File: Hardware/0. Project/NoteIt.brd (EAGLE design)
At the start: 50 x 50 mm, 61 parts, among them CN1 USB 3.2 Gen 2 Type C Receptac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, CN3 Micro-SD Card, CN4 FTSH-105-01-L-DV-K-TR, CN6 Lithium Ion Polymer, IC5 S-8261ACMMD-G4MT2U, Q1 SI2374DS, Q2 SI2374DS, SW1 KY-040, U1 SN74AHC1G125DBV, U2 GL823K, U3 TLV75530PDBVR, U4 TS3A27518EPWR, U8 DS3231/SO

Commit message: board design wip
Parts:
- moved Q1 33.6 mm to (29.0, 25.2), flipped to the bottom
- moved Q2 26.5 mm to (28.7, 29.4), flipped to the bottom
- moved Q4 26.0 mm to (23.4, 22.5), flipped to the bottom
- moved X2 22.4 mm to (28.8, 19.6), turned to 270 degrees
- moved IC2 21.2 mm to (23.9, 25.7), flipped to the bottom, turned to 90 degrees
- moved IC5 20.6 mm to (19.0, 28.9), flipped to the bottom
- moved U1 20.3 mm to (18.8, 23.6), flipped to the bottom
- moved U3 15.2 mm to (23.7, 29.4), flipped to the bottom

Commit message: board design wip
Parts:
- removed CN2: (no value), con-ptr500:AK500/2-H
- added P1: OSTTE020104, Terminal Block 2P 3.5pitch:OST_OSTTE020104
- moved CN4 20.7 mm to (40.5, 17.3)
- moved CN6 16.1 mm to (42.3, 29.6), turned to 270 degrees
- moved U2 15.7 mm to (30.3, 12.0)
- moved U4 13.1 mm to (23.2, 8.77), turned to 180 degrees
- moved SW1 6.78 mm to (40.9, 17.7), turned to 180 degrees
- moved BAT1 6.22 mm to (17.7, 9.16)
- moved CN3 6.22 mm to (8.66, 17.0)
- moved IC2 6.22 mm to (24.1, 19.5)
- moved IC5 6.22 mm to (19.3, 22.7)
- moved Q1 6.22 mm to (29.2, 19.0)
- moved Q4 6.22 mm to (23.7, 16.3)
- moved U1 6.22 mm to (19.1, 17.4)
- moved U10 6.22 mm to (24.9, 21.7)
- moved U3 6.22 mm to (24.0, 23.2)
- moved U8 6.22 mm to (12.6, 21.7)
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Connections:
- net 0V: now also P1.2; no longer CN2.2
- net N$4: now also P1.1; no longer CN2.1
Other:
- board size 50 x 50 mm -> 50 x 35 mm

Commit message: Board design WIP
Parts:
- removed BAT1: CR1220, SamacSys_Parts:1072
- removed P1: OSTTE020104, Terminal Block 2P 3.5pitch:OST_OSTTE020104
- added C12: (no value), My-RLC:C0603
- added CN11: CR1220, SamacSys_Parts:1072
- added CN14: OSTTE020104, Terminal Block 2P 3.5pitch:OST_OSTTE020104
- added R16, R19, R20: (no value), My-RLC:R0603
- moved R6 103.7 mm to (8.26, 1.56), flipped to the bottom
- moved C13 98.4 mm to (8.26, 3.15), flipped to the bottom, turned to 180 degrees
- moved R8 89.9 mm to (18.3, 24.1)
- moved C25 87.4 mm to (11.7, 26.4), flipped to the bottom, turned to 270 degrees
- moved R7 85.9 mm to (18.3, 25.7)
- moved C14 84.8 mm to (12.5, 14.6), turned to 180 degrees
- moved C21 79.3 mm to (18.3, 22.6), turned to 180 degrees
- moved C5 77.8 mm to (18.3, 21.0), turned to 180 degrees
- moved C16 76.6 mm to (35.2, 2.54), flipped to the bottom, turned to 90 degrees
- moved C2 73.2 mm to (26.6, 24.9)
- moved R22 72.4 mm to (15.0, 26.4), flipped to the bottom, turned to 270 degrees
- moved C6 70.5 mm to (26.6, 27.4)
- moved C7 68.7 mm to (33.6, 2.54), flipped to the bottom, turned to 90 degrees
- moved C3 66.6 mm to (16.8, 15.0), flipped to the bottom, turned to 90 degrees
- moved LED2 64.7 mm to (47.6, 7.59), flipped to the bottom, turned to 270 degrees
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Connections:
- net 0V: now also C12.2, CN11.-, CN14.2; no longer BAT1.-, P1.2
- net 3.3V: now also C12.1, R16.1, R19.1, R20.1
- net GPIO_ROTARY_ENCODER_BUTTON: now also R16.2
- net GPIO_ROTARY_ENCODER_SIGNAL_A: now also R19.2
- net GPIO_ROTARY_ENCODER_SIGNAL_B: now also R20.2
- net N$22: now also CN11.+; no longer BAT1.+
- net N$4: now also CN14.1; no longer P1.1
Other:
- board text added: "+"
- board text added: "-"

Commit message: NoteIt v1.0 release
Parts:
- removed C25, C39: (no value), My-RLC:C0603
- removed CN14: OSTTE020104, Terminal Block 2P 3.5pitch:OST_OSTTE020104
- removed IC2: (no value), adafruit:SOT23-5L
- removed IC5: S-8261ACMMD-G4MT2U, SamacSys_Parts:SOT95P275X135-6N
- removed Q4: (no value), transistor-npn:SOT23-BEC
- removed R41, R42: (no value), My-RLC:R0603
- removed U10: (no value), MSP430FR2476TPTR:QFP50P900X900X160-48N
- added C17, C20: 100nF, My-RLC:C0603
- added CN2: Lithium Ion Polymer, Battery:JST-PH-2-SMT-RA
- added Q3: SI2374DS, SI2374DS:SOT-23(TO-236)
- added R21, R23: 10k (5%), My-RLC:R0603
- added U5: SN74AHC1G125DBV, SN74AHC1G125DRLR:SOT23-5
- added U6: TS3A27518EPWR, TS3A27518EPWR:SOP65P640X120-24N
- added U7: TLV75530PDBVR, TLV75530PDBVR:SOT23-5L
- C1: value (none) -> 10uF x 10V
- C10, C5: value (none) -> 10uF
- C11, C12, C15, C16, C19, C2, C21, C4, C6, C7: value (none) -> 100nF
- C13: value (none) -> 1nF x 50V
- C14, C18: value (none) -> 1uF
- C3: value (none) -> 4.7nF
- C8, C9: value (none) -> 22pF x 100V
- CN3: value Micro-SD Card -> (none); device Micro SD:MICROSD-PUSH-OUT -> Terminal Block 2P 3.5pitch:OST_OSTTE020104
- CN6: value Lithium Ion Polymer -> Micro-SD Card; device Battery:JST-PH-2-SMT-RA -> Micro SD:MICROSD-PUSH-OUT
- Q1: value SI2374DS -> BC817; device SI2374DS:SOT-23(TO-236) -> transistor-npn:SOT23-BEC
- R1, R15, R16, R2, R4: value (none) -> 1M
- R10, R19, R20: value (none) -> 4K7 (5%)
- R11: value (none) -> 4k7
- R12: value (none) -> 10k
- R13, R18, R22, R8: value (none) -> 10k (5%)
- R14: value (none) -> 1k (5%)
- R17: value (none) -> 47k (5%)
- R3, R6: value (none) -> 5k1 (5%)
- R5: value (none) -> 4K7
- R7: value (none) -> 2k
- R9: value (none) -> 470R
- U1: value SN74AHC1G125DBV -> MCP73831/2; device SN74AHC1G125DRLR:SOT23-5 -> adafruit:SOT23-5L
- U2: value GL823K -> MSP430FR2476TPTR; device SamacSys_Parts:SOP64P600X175-16N -> MSP430FR2476TPTR:QFP50P900X900X160-48N
- U3: value TLV75530PDBVR -> S-8261ACMMD-G4MT2U; device TLV75530PDBVR:SOT23-5L -> SamacSys_Parts:SOT95P275X135-6N
- U4: value TS3A27518EPWR -> GL823K; device TS3A27518EPWR:SOP65P640X120-24N -> SamacSys_Parts:SOP64P600X175-16N
- Y1: value (none) -> 32.768 kHz
- moved R17 40.1 mm to (8.26, 1.56)
- moved R9 39.8 mm to (15.0, 26.4), turned to 270 degrees
- moved CN3 35.5 mm to (41.0, 30.5), flipped to the top, turned to 180 degrees
- moved C1 32.6 mm to (17.9, 22.6), flipped to the top, turned to 180 degrees
- moved R12 32.1 mm to (47.6, 10.7), turned to 0 degrees
- moved C7 31.3 mm to (13.3, 26.4)
- moved R18 30.9 mm to (16.7, 9.50), turned to 270 degrees
- moved C15 30.8 mm to (18.8, 9.50), turned to 90 degrees
- moved R6 30.5 mm to (38.7, 2.54), turned to 270 degrees
- moved U1 30.2 mm to (17.9, 19.8), turned to 0 degrees
- moved C3 29.6 mm to (43.7, 2.54)
- moved R20 27.1 mm to (17.9, 24.2), flipped to the top, turned to 0 degrees
- moved R22 26.4 mm to (37.1, 11.9)
- moved R19 24.7 mm to (17.9, 25.8), flipped to the top, turned to 0 degrees
- moved C5 23.9 mm to (33.6, 2.54), flipped to the bottom, turned to 90 degrees
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- renumbered C24 to C18, CN11 to CN5, LED2 to LED1, X2 to Y1
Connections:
- net !CONNECT_SDCARD_TO_USB: now also Q1.C, R13.1, U6.14, U6.24; no longer Q4.C, R11.1, U4.14, U4.24
- net !GPIO_DISPLAY_RESET: now also U2.41; no longer U10.41
- net !SDCARD_CARD_DETECT!: now also CN6.9, R18.2, U2.18; no longer CN3.9, R5.2, U10.18
- net !SPI_DISPLAY_CS: now also U2.11; no longer U10.11
- net 0V: now also C1.2, C14.2, C16.2, C17.1, C20.1, C5.1, C6.1, C8.2, CN3.2, CN6.6, CN6.G1, CN6.G2, CN6.G3, CN6.G4, Q1.E, Q3.2, R16.1, R2.1, R4.2, R5.1, R6.2, R7.1, R8.2, U1.2, U2.48, U4.1, U4.14, U5.1, U5.3, U6.20, U6.5, U7.2; no longer C1.1, C14.1, C16.1, C25.2, C39.2, C5.2, C6.2, C7.1, CN14.2, CN3.6, CN3.G1, CN3.G2, CN3.G3, CN3.G4, IC2.2, Q2.2, Q4.E, R1.2, R13.1, R15.2, R18.1, R2.2, R42.1, R9.1, U1.1, U1.3, U10.48, U2.1, U2.14, U3.2, U4.20, U4.5
- net 3.3V: now also C1.1, C15.2, C17.2, C19.1, C2.1, C20.2, CN6.4, R13.2, R17.1, R18.1, R21.1, R22.1, R23.1, U2.1, U5.5, U6.8, U7.5; no longer C14.2, C25.1, C3.2, C39.1, C4.2, C5.1, CN3.4, R11.2, R16.1, R5.1, R6.1, R7.1, R8.1, U1.5, U10.1, U3.5, U4.8
- net ADC_BATTERY_VOLTAGE: now also R15.1, R16.2, U2.12; no longer R41.1, R42.2, U10.12
- net GPIO_BATTERY_CHARGING_STATUS: now also U1.1, U2.42; no longer IC2.1, U10.42
- net GPIO_DISPLAY_TRANSMISSION_MODE: now also U2.32; no longer U10.32
- net GPIO_ROTARY_ENCODER_BUTTON: now also R21.2, U2.33; no longer R16.2, U10.33
- net GPIO_ROTARY_ENCODER_SIGNAL_A: now also R22.2, U2.34; no longer R19.2, U10.34
- net GPIO_ROTARY_ENCODER_SIGNAL_B: now also R23.2, U2.35; no longer R20.2, U10.35
- net GPIO_USB_DETECT: now also R1.1, R2.2, U2.17; no longer R4.1, R9.2, U10.17
- net I2C_RTC_SCL: now also R20.2, U2.15; no longer R8.2, U10.15
- net I2C_RTC_SDA: now also R19.2, U2.14; no longer R7.2, U10.14
- net ICSP_SBWTCK: now also U2.3; no longer U10.3
- net ICSP_SBWTDIO: now also R17.2, U2.2; no longer R6.2, U10.2
- net MCU_!SPI_SDCARD_CS: now also U2.7, U6.16; no longer U10.7, U4.16
- net MCU_SPI_SDCARD_SCLK: now also U2.6, U6.11; no longer U10.6, U4.11
- net MCU_SPI_SDCARD_SIMO: now also U2.4, U6.13; no longer U10.4, U4.13
- net MCU_SPI_SDCARD_SOMI: now also U2.5, U6.15; no longer U10.5, U4.15
- net N$1: now also Q2.1, U3.1; no longer IC5.1, Q1.1
- net N$10: now also C3.2, R4.1; no longer C1.2, R3.1
- net N$11: now also R11.1, R14.1, U4.13, U4.9; no longer R10.1, R17.1, U2.13, U2.9
- net N$12: now also R11.2, R12.2, U4.11; no longer R10.2, R18.2, U2.11
- net N$13: now also C6.2, U4.8; no longer C15.2, U2.8
- net N$14: now also Q1.B, R10.1; no longer Q4.B, R14.1
- net N$15: now also CN6.3, U6.6; no longer CN3.3, U4.6
- net N$16: now also CN6.7, U6.7; no longer CN3.7, U4.7
- net N$2: now also CN6.5, U6.4; no longer CN3.5, U4.4
- net N$20: now also CN6.8, U6.9; no longer CN3.8, U4.9
- net N$21: now also R6.1; no longer R2.1
- net N$26: now also R5.2, U1.5; no longer IC2.5, R12.2
- net N$27: now also Q3.1, U3.3; no longer IC5.3, Q2.1
- net N$29: now also R7.2, U3.2; no longer IC5.2, R13.2
- net N$3: now also Q3.3; no longer Q1.3
- net N$31: now also C7.1, R9.2, U3.5; no longer C8.1, IC5.5, R22.2
- net N$32: now also C7.2, CN2.2, Q2.2, U3.6; no longer C8.2, CN6.2, IC5.6, Q1.2
- net N$33: now also C14.1, C16.1, CN2.1, R15.2, R9.1, U1.3, U7.1, U7.3; no longer C19.1, C9.1, CN6.1, IC2.3, R22.1, R41.2, U3.1, U3.3
- net N$4: now also CN3.1, U5.2; no longer CN14.1, U1.2
- net N$5: now also U4.12; no longer U2.12
- net N$6: now also R3.1; no longer R1.1
- net N$7: now also CN6.1, U6.10; no longer CN3.1, U4.10
- net N$8: now also CN6.2, U6.12; no longer CN3.2, U4.12
- net N$9: now also R14.2; no longer R17.2
- net SPI_DISPLAY_SCLK: now also U2.10; no longer U10.10
- net SPI_DISPLAY_SIMO: now also U2.9; no longer U10.9
- net UART_DATALOGGER_RX: now also U2.29, U5.4; no longer U1.4, U10.29
- net USB_CLK: now also U4.4, U6.2; no longer U2.4, U4.2
- net USB_CMD: now also U4.5, U6.1; no longer U2.5, U4.1
- net USB_DAT0: now also U4.3, U6.23; no longer U2.3, U4.23
- net USB_DAT1: now also U4.2, U6.21; no longer U2.2, U4.21
- net USB_DAT2: now also U4.7, U6.19; no longer U2.7, U4.19
- net USB_DAT3: now also U4.6, U6.22; no longer U2.6, U4.22
- net USB_N: now also U4.15; no longer U2.15
- net USB_P: now also U4.16; no longer U2.16
- net VUSB: now also C4.2, C5.2, R1.2, R10.2, R8.1, U1.4, U4.10; no longer C16.2, C7.2, IC2.4, R14.2, R15.1, R4.2, U2.10
- net XTAL_IN: now also C8.1, U2.46; no longer C2.1, U10.46
- net XTAL_OUT: now also C9.1, U2.47; no longer C6.1, U10.47
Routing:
- net 3.3V: track 0.00 -> 179.5 mm, vias 0 -> 6
- net VUSB: track 0.00 -> 78.9 mm, vias 0 -> 4
- net N$33: track 0.00 -> 47.3 mm, vias 0 -> 3
- net N$32: track 0.00 -> 39.5 mm, vias 0 -> 4
- net GPIO_USB_DETECT: track 0.00 -> 38.2 mm, vias 0 -> 2
- net I2C_RTC_SCL: track 0.00 -> 37.9 mm, vias 0 -> 3
- net N$22: track 0.00 -> 36.4 mm, vias 0 -> 2
- net ICSP_SBWTDIO: track 0.00 -> 33.5 mm, vias 0 -> 3
- net 0V: track 0.00 -> 33.2 mm, vias 0 -> 138
- net I2C_RTC_SDA: track 0.00 -> 32.3 mm, vias 0 -> 3
- net USB_CMD: track 0.00 -> 32.3 mm, vias 0 -> 2
- net USB_CLK: track 0.00 -> 28.4 mm, vias 0 -> 2
- net USB_DAT3: track 0.00 -> 28.2 mm, vias 0 -> 2
- net USB_DAT2: track 0.00 -> 27.1 mm, vias 0 -> 2
- net GPIO_ROTARY_ENCODER_SIGNAL_B: track 0.00 -> 26.2 mm, vias 0 -> 1
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- added copper zone on layer 1, net 0V
- added copper zone on layer 15, net 0V
- added copper zone on layer 16, net 0V
- added copper zone on layer 2, net 0V
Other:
- board text added: "GND"
- board text added: "IN"
- board text added: "NoteIt v1.0"

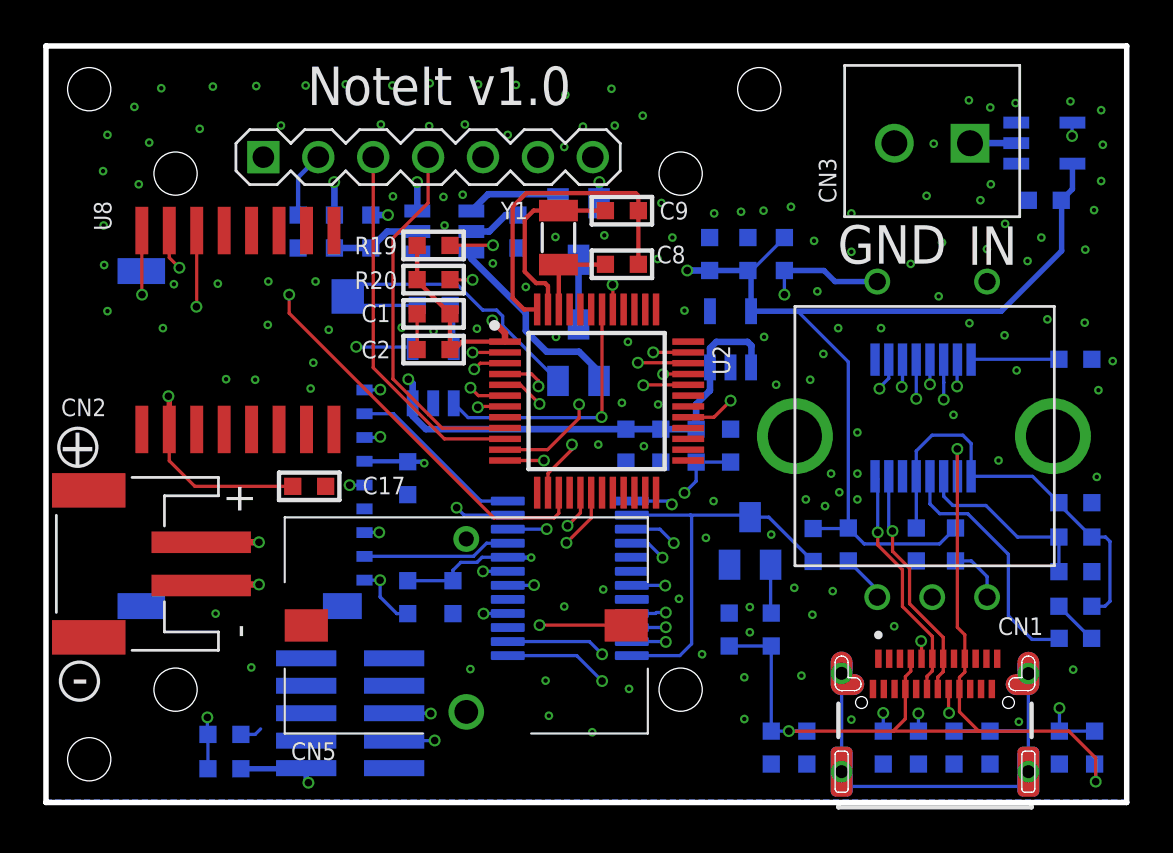
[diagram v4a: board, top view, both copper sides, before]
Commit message: NoteIt v1.1 release (details in commit description)
- Vias with 0.2mm and 0.4mm diameter drill changed to 0.3mm and 0.6mm diameter drill.
- The first approach makes the production of PCBs much more expensive (JLCPCB experience).
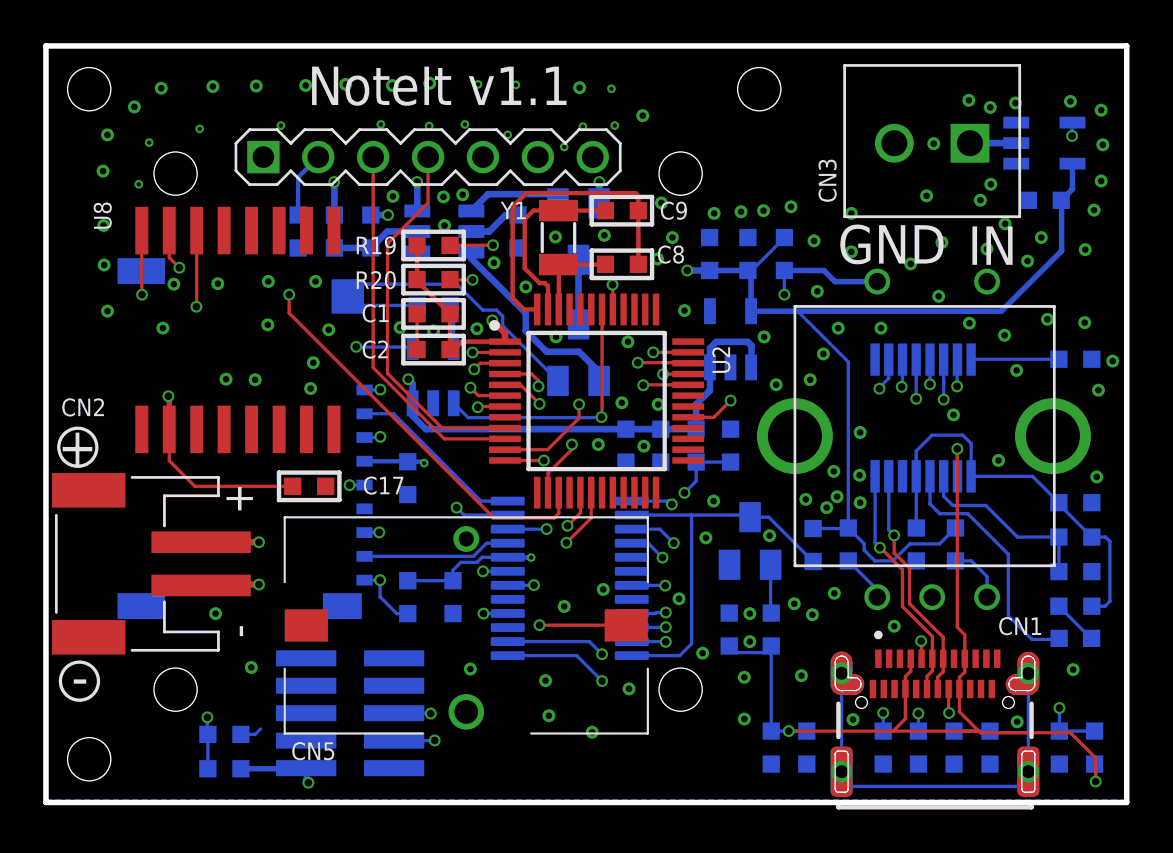
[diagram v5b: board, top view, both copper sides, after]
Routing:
- net 3.3V: track 179.5 -> 180.3 mm
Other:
- board text added: "NoteIt v1.1"
- board text removed: "NoteIt v1.0"

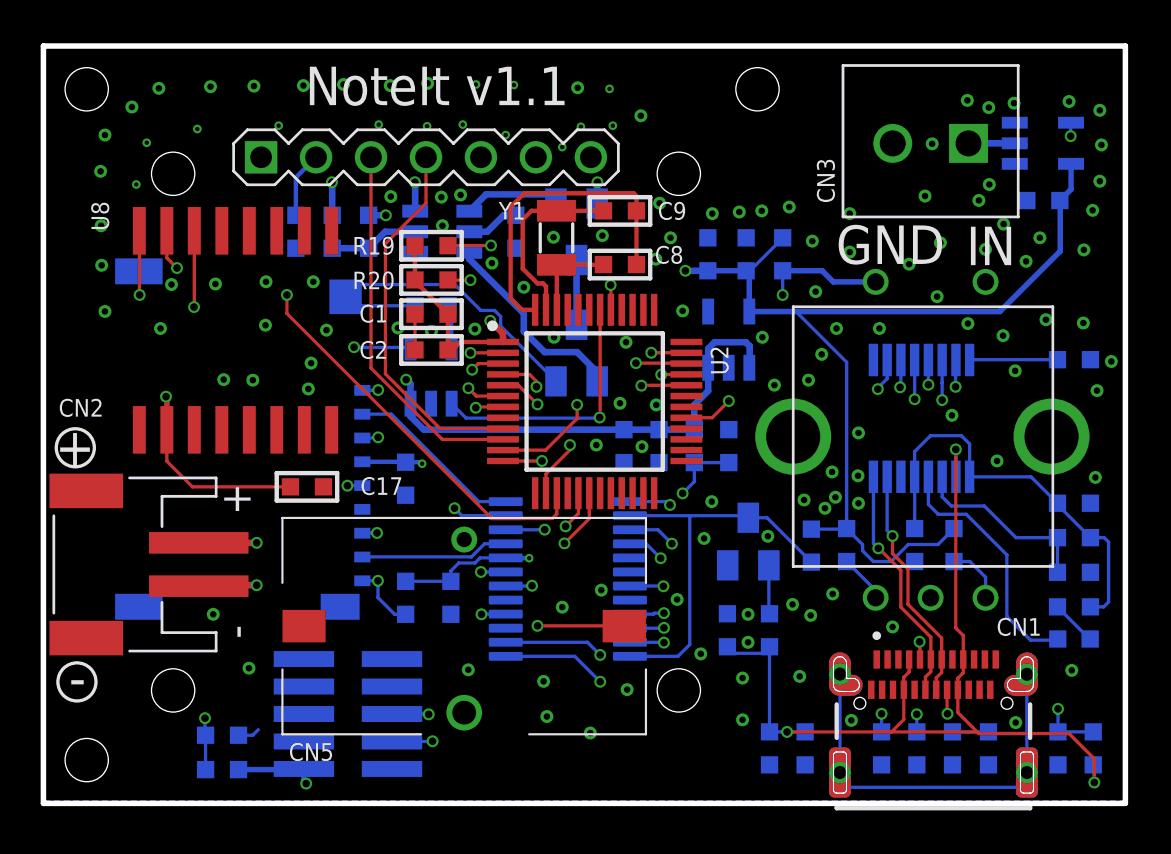
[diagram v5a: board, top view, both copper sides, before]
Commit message: NoteIt v1.2 release (details in commit description)
- All vias changed to 0.3mm drill with 0.6mm diameter.
- This approach saves money in the production of PCBs (JLCPCB experience) - less tests is necessary.
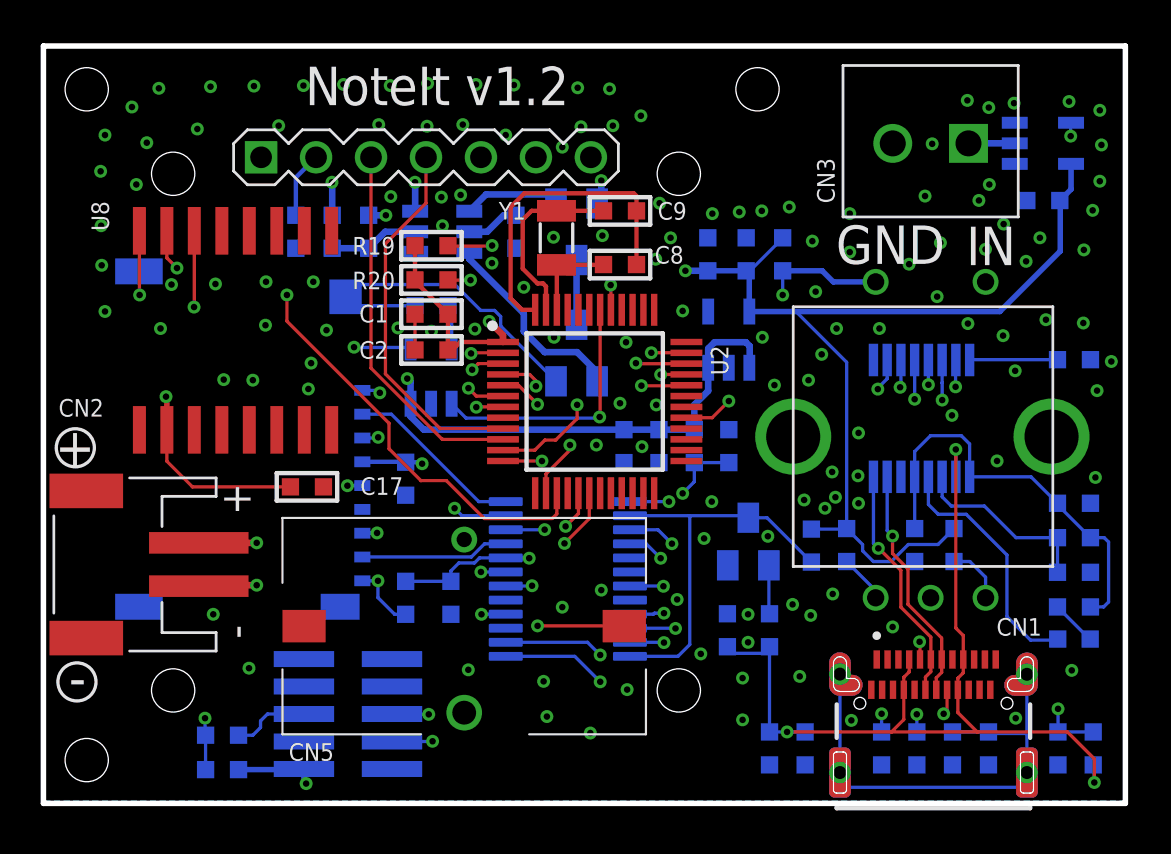
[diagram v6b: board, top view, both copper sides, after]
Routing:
- net 0V: track 33.2 -> 35.8 mm
- net I2C_RTC_SCL: track 37.9 -> 38.8 mm
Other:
- board text added: "NoteIt v1.2"
- board text removed: "NoteIt v1.1"
